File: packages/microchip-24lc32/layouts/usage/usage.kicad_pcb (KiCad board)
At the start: 2 copper layers, 4 parts

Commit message: many packages building
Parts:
- C1: value 100nF ±10% 16V X7R -> 1.0000000000000001e-07F
- R1, R2: value 10kΩ ±1% 62.5mW -> 10000.0Ω
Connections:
- net GND renamed lv
- net VCC renamed eeprom-power-hv-0

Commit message: review tool updates
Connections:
- net eeprom-power-hv-0 renamed hv
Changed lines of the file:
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@@
 			(usegerberadvancedattributes yes)
 			(creategerberjobfile yes)
-			(dashed_line_dash_ratio 12.000000)
-			(dashed_line_gap_ratio 3.000000)
+			(dashed_line_dash_ratio 12)
+			(dashed_line_gap_ratio 3)
 			(svgprecision 4)
 			(plotframeref no)
@@
 			(hpglpennumber 1)
 			(hpglpenspeed 20)
-			(hpglpendiameter 15.000000)
+			(hpglpendiameter 15)
 			(pdf_front_fp_property_popups yes)
 			(pdf_back_fp_property_popups yes)
@@
 	(net 0 "")
 	(net 1 "lv")
-	(net 2 "eeprom-power-hv-0")
+	(net 2 "hv")
 	(net 3 "SDA")
 	(net 4 "WP")
@@
 			(size 0.57 0.54)
 			(layers "F.Cu" "F.Paste" "F.Mask")
-			(net 2 "eeprom-power-hv-0")
+			(net 2 "hv")
 		)
 		(pad "1" smd rect
@@
 			(size 0.57 0.54)
 			(layers "F.Cu" "F.Paste" "F.Mask")
-			(net 2 "eeprom-power-hv-0")
+			(net 2 "hv")
 		)
 		(pad "1" smd rect
@@
 			(size 0.5 0.54)
 			(layers "F.Cu" "F.Paste" "F.Mask")
-			(net 2 "eeprom-power-hv-0")
+			(net 2 "hv")
 		)
 		(embedded_fonts no)
@@
 			(size 1 0.6)
 			(layers "F.Cu" "F.Mask" "F.Paste")
-			(net 2 "eeprom-power-hv-0")
+			(net 2 "hv")
 		)
 		(pad "5" smd rect

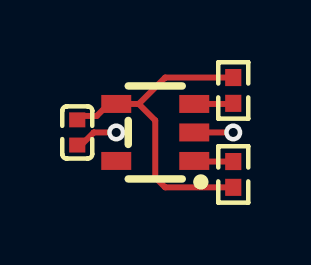
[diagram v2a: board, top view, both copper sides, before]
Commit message: remove all those other changes, just bosch baby
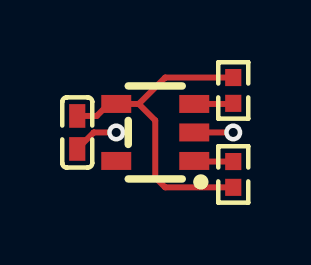
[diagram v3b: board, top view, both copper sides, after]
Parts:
- C1: value 1.0000000000000001e-07F -> 100nF ±10% 16V X7R
- R1, R2: value 10000.0Ω -> 10kΩ ±1% 62.5mW
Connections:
- net hv renamed VCC
- net lv renamed GND
